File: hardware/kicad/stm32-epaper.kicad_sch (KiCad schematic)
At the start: 0 parts

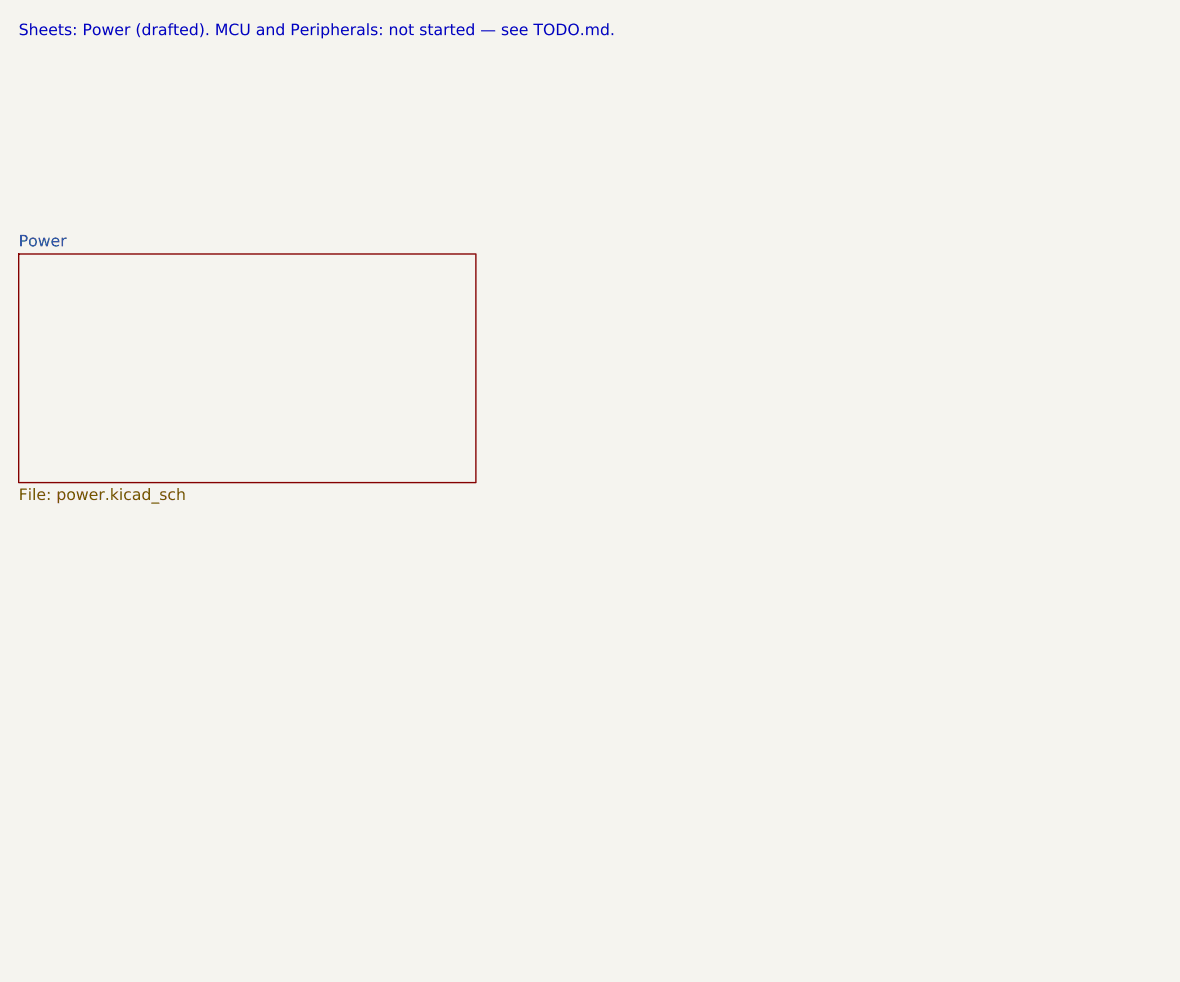
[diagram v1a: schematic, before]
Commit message: Add MCU, Memory and Peripherals sheets; whole-schematic checker
- MCU (A2): STM32F469IIT6 LQFP176. Pin assignment lives in
  sheet_mcu.PINMAP and follows the F469-Disco (FMC SDRAM now 16-bit, QSPI,
  SDIO, SPI1 + HAT control pins, USART3 log UART, I2C1) so the firmware
  config carries over. SD card-detect moved PG2 -> PG10 to keep EXTI2 for
  HRDY. DS11189 power scheme: 13x100nF + 4.7uF, VDDUSB, ferrite-fed
  VDDA/VREF+, 2x2.2uF VCAP; DSI unused per DS11189 2.18 (VDDDSI->VDD,
  VCAPDSI->VDD12DSI, no cap). 8 MHz HSE, 32.768 kHz LSE, BOOT button for
  ROM DFU (BOOT1/PB2 pulled low), TC2050 SWD+SWO, UART header, status LED,
  1k series on the PA9 VBUS sense.
- Memory: IS42S16400J (8 MB), W25Q128JV QSPI, Molex 104031-0811 microSD
  with detect switch and 47k pull-ups, all on 3V3_PERIPH.
- Peripherals: 1x8 header for the external IT8951 HAT (33R series on
  SCK/MOSI/CS), CAP1188 (I2C addr 0x29, 4 electrode pads), PEC11R encoder
  with Bourns' filter, WKUP power button (active high).
- New project symbol CAP1188 and footprint PEC11R-4xxxF-Sxxxx (datasheet
  PCB layout; the Alps EC11E footprint does not fit, its tabs are 11.2 mm
  apart vs 13.2 mm).
- Generator split into common.py + one module per sheet (gen_schematic.py);
  check_schematic.py replaces check_power_netlist.py and adds pin-mux
  (required alternate function per pin), memory-bus end-to-end,
  single-connection-net and pin-vs-footprint-pad checks.

ERC: 0 violations. check_schematic.py: 187 nets, 83 MCU pins, 604 pin/pad
connections OK. All 83 assigned pin numbers also cross-checked by hand
against the DS11189 LQFP176 pin table.

Co-Authored-By: Claude Opus 5.5 <noreply@anthropic.com>
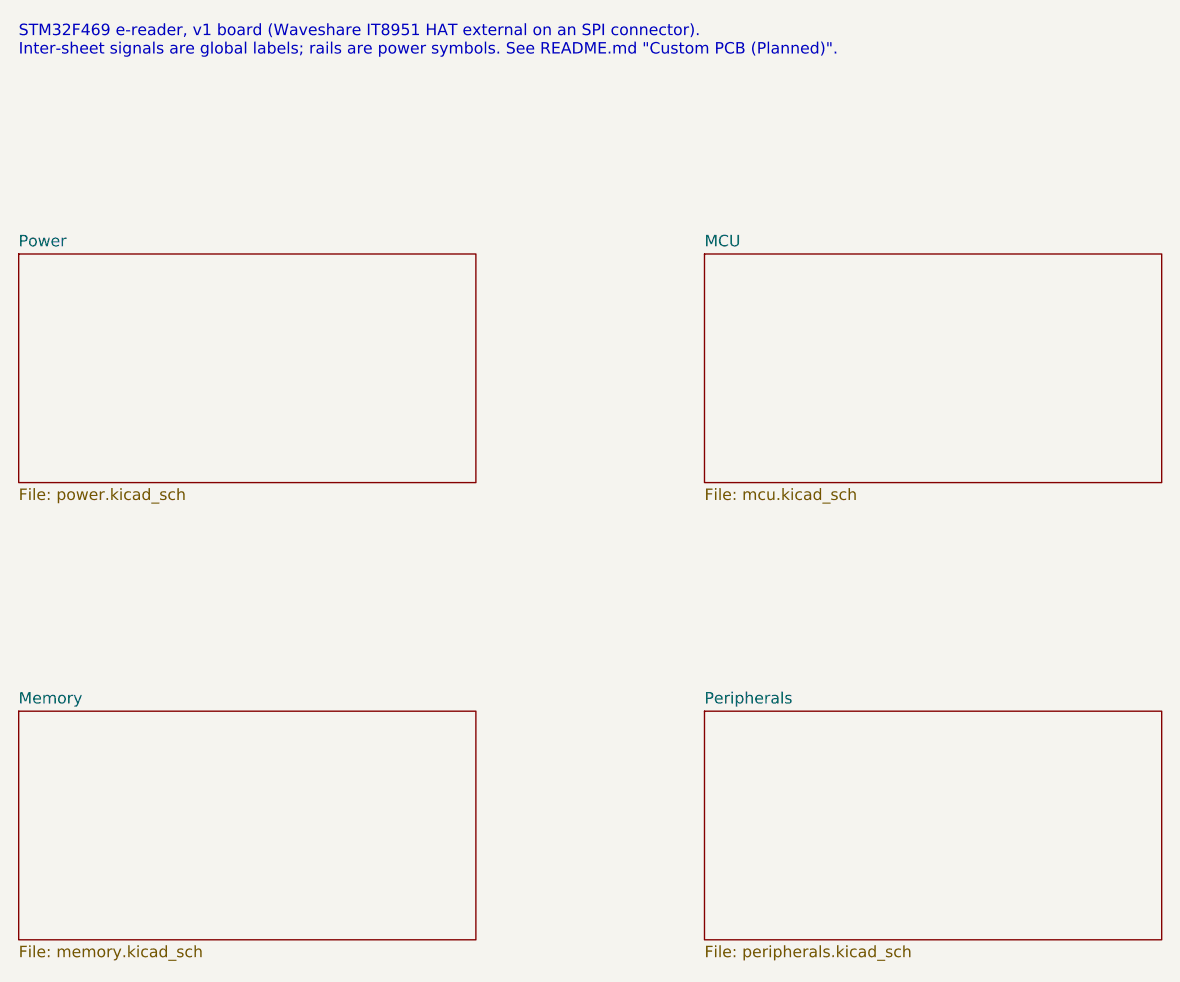
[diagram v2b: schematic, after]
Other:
- added sheet MCU (mcu.kicad_sch)
- added sheet Memory (memory.kicad_sch)
- added sheet Peripherals (peripherals.kicad_sch)
- note added: "STM32F469 e-reader, v1 board (Waveshare IT8951 HAT external on an SPI connector). Inter-sheet signals are global labels; rails are power symbols. See README.md "Custom PCB (Planned)"."
- note removed: "Sheets: Power (drafted). MCU and Peripherals: not started — see TODO.md."
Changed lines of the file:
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@@
 		(title "STM32 e-reader")
 	)
-	(text "Sheets: Power (drafted). MCU and Peripherals: not started — see TODO.md."
+	(text "STM32F469 e-reader, v1 board (Waveshare IT8951 HAT external on an SPI connector).\nInter-sheet signals are global labels; rails are power symbols. See README.md \"Custom PCB (Planned)\"."
 		(exclude_from_sim no)
 		(at 25.4 25.4 0)
@@
 				)
 			)
+		)
+	)
+	(sheet
+		(at 101.6 50.8)
+		(size 50.8 25.4)
+		(exclude_from_sim no)
+		(in_bom yes)
+		(on_board yes)
+		(dnp no)
+		(stroke
+			(width 0.1524)
+			(type solid)
+		)
+		(fill
+			(color 0 0 0 0)
+		)
+		(property "Sheetname" "MCU"
+			(at 101.6 50.1 0)
+			(effects
+				(font
+					(size 1.27 1.27)
+				)
+				(justify left bottom)
+			)
+		)
+		(property "Sheetfile" "mcu.kicad_sch"
+			(at 101.6 76.8 0)
+			(effects
+				(font
+					(size 1.27 1.27)
+				)
+				(justify left top)
+			)
+		)
+		(instances
+			(project "stm32-epaper"
+				(path "/6f1d3c2a-5b7e-4c1d-9a0f-000000000001"
+					(page "3")
+				)
+			)
+		)
+	)
+	(sheet
+		(at 25.4 101.6)
+		(size 50.8 25.4)
+		(exclude_from_sim no)
+		(in_bom yes)
+		(on_board yes)
+		(dnp no)
+		(stroke
+			(width 0.1524)
+			(type solid)
+		)
+		(fill
+			(color 0 0 0 0)
+		)
+		(property "Sheetname" "Memory"
+			(at 25.4 100.9 0)
+			(effects
+				(font
+					(size 1.27 1.27)
+				)
+				(justify left bottom)
+			)
+		)
+		(property "Sheetfile" "memory.kicad_sch"
+			(at 25.4 127.6 0)
+			(effects
+				(font
+					(size 1.27 1.27)
+				)
+				(justify left top)
+			)
+		)
+		(instances
+			(project "stm32-epaper"
+				(path "/6f1d3c2a-5b7e-4c1d-9a0f-000000000001"
+					(page "4")
+				)
+			)
+		)
+	)
+	(sheet
+		(at 101.6 101.6)
+		(size 50.8 25.4)
+		(exclude_from_sim no)
+		(in_bom yes)
+		(on_board yes)
+		(dnp no)
+		(stroke
+			(width 0.1524)
+			(type solid)
+		)
+		(fill
+			(color 0 0 0 0)
+		)
+		(property "Sheetname" "Peripherals"
+			(at 101.6 100.9 0)
+			(effects
+				(font
+					(size 1.27 1.27)
+				)
+				(justify left bottom)
+			)
+		)
+		(property "Sheetfile" "peripherals.kicad_sch"
+			(at 101.6 127.6 0)
+			(effects
+				(font
+					(size 1.27 1.27)
+				)
+				(justify left top)
+			)
+		)
+		(instances
+			(project "stm32-epaper"
+				(path "/6f1d3c2a-5b7e-4c1d-9a0f-000000000001"
+					(page "5")
+				)
+			)
